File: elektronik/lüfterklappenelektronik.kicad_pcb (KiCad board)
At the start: 2 copper layers, 26 parts, among them P101 CONN_01X04, P103 PressureSensor3, P104 PressureSensor2, P105 PressureSensor1, P106 DamperMotor1, P107 DamperMotor2, P108 DamperMotor3, P109 CONN_01X03, Q101 IRF9540N, Q102 IRF9540N, Q103 IRF9540N, U101 Gabellichtschranke, U102 Gabellichtschranke, U103 Gabellichtschranke, U104 ZG3NC-240B, U105 ATMEGA32U4-A

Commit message: some never to be used routing
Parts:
- P103: footprint Pin_Headers:Pin_Header_Straight_1x04 -> Pin_Headers:Pin_Header_Straight_1x06
- P104: value PressureSensor2 -> PressureSensor1; footprint Pin_Headers:Pin_Header_Straight_1x04 -> Pin_Headers:Pin_Header_Straight_1x06
- P105: value PressureSensor1 -> PressureSensor2; footprint Pin_Headers:Pin_Header_Straight_1x04 -> Pin_Headers:Pin_Header_Straight_1x06
- moved P101 6.25 mm to (127.6, 80.0)
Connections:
- P103 pad 1: /PS3SS -> +5V
- P103 pad 2: Net-(P103-Pad2) -> GND
- P103 pad 3: Net-(P103-Pad3) -> /PS3SS
- P104 pad 1: /PS2SS -> +5V
- P104 pad 2: Net-(P103-Pad2) -> GND
- P104 pad 3: Net-(P103-Pad3) -> /PS1SS
- P105 pad 1: /PS1SS -> +5V
- P105 pad 2: Net-(P103-Pad2) -> GND
- P105 pad 3: Net-(P103-Pad3) -> /PS2SS
- U105 pad 10: Net-(P103-Pad3) -> Net-(P103-Pad5)
- U105 pad 11: Net-(P103-Pad4) -> Net-(P103-Pad6)
- U105 pad 9: Net-(P103-Pad2) -> Net-(P103-Pad4)
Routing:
- net +5V: track 0.00 -> 31.8 mm
- net Net-(P103-Pad6): track 0.00 -> 21.9 mm
- net Net-(P103-Pad5): track 0.00 -> 15.6 mm
- net Net-(P103-Pad2): track 13.8 -> 0.00 mm
- net Net-(P103-Pad3): track 12.7 -> 0.00 mm
- net GND: track 45.7 -> 57.9 mm
- net /PJON: track 0.00 -> 11.3 mm
- net /PS2SS: track 23.2 -> 32.2 mm
- net /PS3SS: track 30.0 -> 32.1 mm
- net /PS1SS: track 27.9 -> 27.2 mm

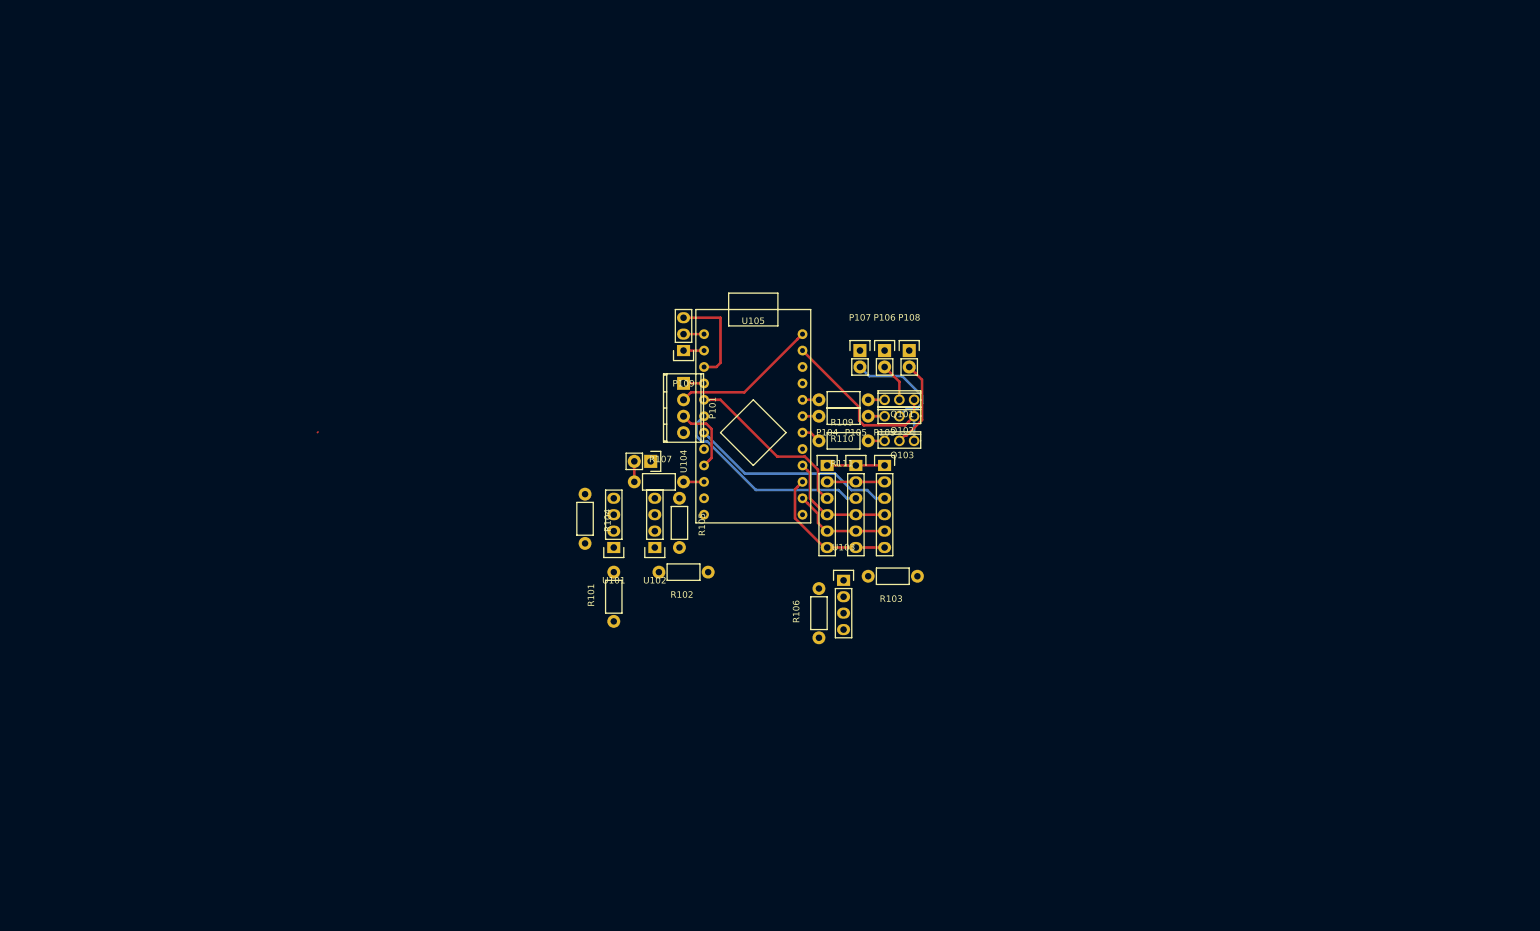
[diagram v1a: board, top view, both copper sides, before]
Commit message: fixed footprints of R and Diode
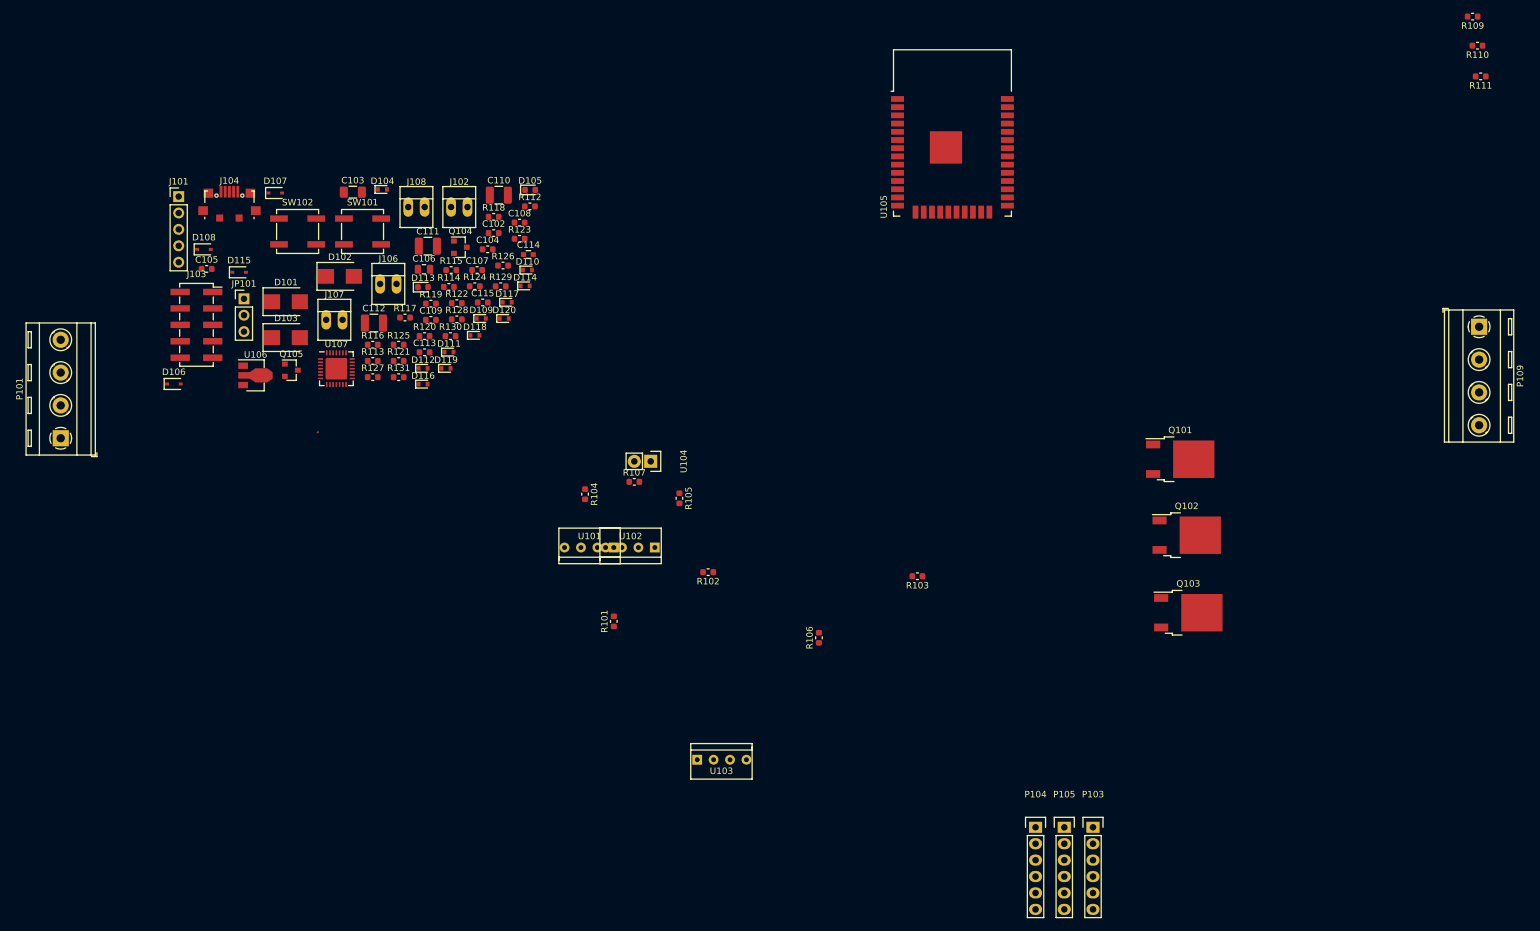
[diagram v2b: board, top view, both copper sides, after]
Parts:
- removed P106: DamperMotor1, Pin_Headers:Pin_Header_Straight_1x02
- removed P107: DamperMotor2, Pin_Headers:Pin_Header_Straight_1x02
- removed P108: DamperMotor3, Pin_Headers:Pin_Header_Straight_1x02
- added C102: 100nF/50V, Capacitor_SMD:C_0603_1608Metric, F.Cu at (98.2, 56.8)
- added C103: 220µF/6.3V(20%), Capacitor_SMD:C_1206_3216Metric, F.Cu at (76.5, 50.4)
- added C104: 100nF/50V, Capacitor_SMD:C_0603_1608Metric, F.Cu at (97.3, 59.3)
- added C105: 1µF/50V, Capacitor_SMD:C_0603_1608Metric, F.Cu at (53.8, 62.3)
- added C106: 10µF/25V, Capacitor_SMD:C_0805_2012Metric, F.Cu at (87.5, 62.4)
- added C107: 100nF/50V, Capacitor_SMD:C_0603_1608Metric, F.Cu at (95.7, 62.5)
- added C108: 100nF/50V, Capacitor_SMD:C_0603_1608Metric, F.Cu at (102.3, 55.1)
- added C109: 100nF/50V, Capacitor_SMD:C_0603_1608Metric, F.Cu at (88.5, 70.2)
- added C110: 22uF/25V(10%), Capacitor_SMD:C_1210_3225Metric, F.Cu at (99.0, 50.9)
- added C111: 22uF/25V(10%), Capacitor_SMD:C_1210_3225Metric, F.Cu at (88.1, 58.8)
- added C112: 22uF/25V(10%), Capacitor_SMD:C_1210_3225Metric, F.Cu at (79.7, 70.7)
- added C113: 100nF/50V, Capacitor_SMD:C_0603_1608Metric, F.Cu at (87.6, 75.2)
- added C114: 4.7µF/6.3V(10%), Capacitors_SMD:C_0603, F.Cu at (103.6, 60.1)
- added C115: 100nF/50V, Capacitor_SMD:C_0603_1608Metric, F.Cu at (96.6, 67.5)
- added D101: D_Schottky, Diode_SMD:D_SMB, F.Cu at (66.1, 67.4)
- added D102: D_Schottky, Diode_SMD:D_SMB, F.Cu at (74.5, 63.5)
- added D103: D_Schottky, Diode_SMD:D_SMB, F.Cu at (66.1, 72.9)
- added D104: LESD5D5.0CT1G, Diode_SMD:D_SOD-523, F.Cu at (81.0, 50.0)
- added D105: GREEN_LED, LED_SMD:LED_0603_1608Metric, F.Cu at (103.9, 50.1)
- added D106: BAT760-7, Diode_SMD:D_SOD-323, F.Cu at (48.8, 80.1)
- added D107: BAT760-7, Diode_SMD:D_SOD-323, F.Cu at (64.5, 50.5)
- added D108: BAT760-7, Diode_SMD:D_SOD-323, F.Cu at (53.4, 59.3)
- added D109: LESD5D5.0CT1G, Diode_SMD:D_SOD-523, F.Cu at (96.3, 70.0)
- added D110: LESD5D5.0CT1G, Diode_SMD:D_SOD-523, F.Cu at (103.5, 62.5)
- added D111: LESD5D5.0CT1G, Diode_SMD:D_SOD-523, F.Cu at (91.3, 75.2)
- added D112: LESD5D5.0CT1G, Diode_SMD:D_SOD-523, F.Cu at (87.3, 77.7)
- added D113: GREEN_LED, LED_SMD:LED_0603_1608Metric, F.Cu at (87.3, 65.1)
- added D114: LESD5D5.0CT1G, Diode_SMD:D_SOD-523, F.Cu at (103.1, 64.9)
- added D115: BAT760-7, Diode_SMD:D_SOD-323, F.Cu at (58.9, 62.8)
- added D116: LESD5D5.0CT1G, Diode_SMD:D_SOD-523, F.Cu at (87.3, 80.1)
- added D117: LESD5D5.0CT1G, Diode_SMD:D_SOD-523, F.Cu at (100.3, 67.5)
- added D118: LESD5D5.0CT1G, Diode_SMD:D_SOD-523, F.Cu at (95.3, 72.6)
- added D119: LESD5D5.0CT1G, Diode_SMD:D_SOD-523, F.Cu at (90.9, 77.7)
- added D120: LESD5D5.0CT1G, Diode_SMD:D_SOD-523, F.Cu at (99.9, 70.0)
- added J101: Conn_01x05_Male, Connector_PinHeader_2.54mm:PinHeader_1x05_P2.54mm_Vertical, F.Cu at (49.5, 51.1)
- added J102: Ckmtw_2510S-2P, Connect:PINHEAD1-2, F.Cu at (91.7, 52.7)
- added J103: Conn_LAN_ENC28J60, Connector_PinSocket_2.54mm:PinSocket_2x05_P2.54mm_Vertical_SMD, F.Cu at (52.3, 71.0)
- added J104: USB_B_Micro, FootprintsTittelbach:USB_Micro-B_C77238, F.Cu at (57.4, 52.0)
- added J106: Ckmtw_2510S-2P, Connect:PINHEAD1-2, F.Cu at (80.7, 64.6)
- added J107: Ckmtw_2510S-2P, Connect:PINHEAD1-2, F.Cu at (72.3, 70.2)
- added J108: Ckmtw_2510S-2P, Connect:PINHEAD1-2, F.Cu at (85.0, 52.7)
- added JP101: Jumper µC Supply, Connector_PinHeader_2.54mm:PinHeader_1x03_P2.54mm_Vertical, F.Cu at (59.6, 66.9)
- added Q104: Q_NPN_Darlington_BEC, Package_TO_SOT_SMD:SOT-23, F.Cu at (93.1, 58.9)
- added Q105: Q_NPN_Darlington_BEC, Package_TO_SOT_SMD:SOT-23, F.Cu at (66.9, 78.0)
- added R112: 110(1%), Resistor_SMD:R_0603_1608Metric, F.Cu at (103.9, 52.6)
- added R113: 0R(5%), Resistor_SMD:R_0603_1608Metric, F.Cu at (79.5, 76.5)
- added R114: 0R(5%), Resistor_SMD:R_0603_1608Metric, F.Cu at (91.3, 65.1)
- added R115: 10K(5%), Resistor_SMD:R_0603_1608Metric, F.Cu at (91.7, 62.5)
- added R116: 10K(5%), Resistor_SMD:R_0603_1608Metric, F.Cu at (79.5, 74.0)
- added R117: 10K(5%), Resistor_SMD:R_0603_1608Metric, F.Cu at (84.5, 69.8)
- added R118: 22(1%), Resistor_SMD:R_0603_1608Metric, F.Cu at (98.2, 54.2)
- added R119: 22(1%), Resistor_SMD:R_0603_1608Metric, F.Cu at (88.5, 67.7)
- added R120: 22(1%), Resistor_SMD:R_0603_1608Metric, F.Cu at (87.6, 72.7)
- added R121: 22(1%), Resistor_SMD:R_0603_1608Metric, F.Cu at (83.5, 76.5)
- added R122: 22(1%), Resistor_SMD:R_0603_1608Metric, F.Cu at (92.5, 67.6)
- added R123: 22(1%), Resistor_SMD:R_0603_1608Metric, F.Cu at (102.3, 57.6)
- added R124: 22(1%), Resistor_SMD:R_0603_1608Metric, F.Cu at (95.3, 65.0)
- added R125: 2K, Resistor_SMD:R_0603_1608Metric, F.Cu at (83.5, 74.0)
- added R126: 22.1K(5%), Resistor_SMD:R_0603_1608Metric, F.Cu at (99.7, 61.8)
- added R127: 47.5K(5%), Resistor_SMD:R_0603_1608Metric, F.Cu at (79.5, 79.0)
- added R128: 2K(5%), Resistor_SMD:R_0603_1608Metric, F.Cu at (92.5, 70.1)
- added R129: 22(1%), Resistor_SMD:R_0603_1608Metric, F.Cu at (99.3, 65.0)
- added R130: 22(1%), Resistor_SMD:R_0603_1608Metric, F.Cu at (91.6, 72.7)
- added R131: 10K(5%), Resistor_SMD:R_0603_1608Metric, F.Cu at (83.5, 79.0)
- added SW101: SW_Push, Button_Switch_SMD:SW_SPST_B3SL-1022P, F.Cu at (78.0, 56.5)
- added SW102: SW_Push, Button_Switch_SMD:SW_SPST_B3SL-1022P, F.Cu at (67.9, 56.5)
- added U106: AMS1117-3.3, Package_TO_SOT_SMD:SOT-89-3, F.Cu at (61.0, 78.8)
- added U107: CP2102N-A01-GQFN28, Package_DFN_QFN:QFN-28-1EP_5x5mm_P0.5mm_EP3.35x3.35mm, F.Cu at (73.9, 77.7)
- P101: value CONN_01X04 -> PWR_BUS_CONN1; footprint Terminal_Blocks:TerminalBlock_Pheonix_MPT-2.54mm_4pol -> TerminalBlock_RND:TerminalBlock_RND_205-00289_1x04_P5.08mm_Horizontal
- P109: value CONN_01X03 -> PWR_BUS_CONN2; footprint Pin_Headers:Pin_Header_Straight_1x03 -> TerminalBlock_RND:TerminalBlock_RND_205-00289_1x04_P5.08mm_Horizontal
- Q101, Q102, Q103: value IRF9540N -> IRLR8743TRPBF; footprint TO_SOT_Packages_THT:TO-251AA -> Package_TO_SOT_SMD:TO-252-2
- R101, R102, R103: value 120 -> 43(1%); footprint Resistors_ThroughHole:Resistor_Horizontal_RM7mm -> Resistor_SMD:R_0603_1608Metric
- R104, R105, R106: footprint Resistors_ThroughHole:Resistor_Horizontal_RM7mm -> Resistor_SMD:R_0603_1608Metric
- R107: value 100 -> 160(1%); footprint Resistors_ThroughHole:Resistor_Horizontal_RM7mm -> Resistor_SMD:R_0603_1608Metric
- R109, R110, R111: value 100 -> 100(1%); footprint Resistors_ThroughHole:Resistor_Horizontal_RM7mm -> Resistor_SMD:R_0603_1608Metric
- U101, U102, U103: footprint Pin_Headers:Pin_Header_Straight_1x04 -> FootprintsTittelbach:Ckmtw_2510S-4P
- U105: value ATMEGA32U4-A -> ESP32-WROOM-32E; footprint ArduinoTeensyFootprints:ArduProMicro -> RF_Module:ESP32-WROOM-32
- moved P109 123.2 mm to (250.8, 71.2), turned to 270 degrees
- moved R109 110.8 mm to (249.8, 23.2)
- moved R110 110.4 mm to (250.5, 27.8)
- moved R111 110.3 mm to (251.0, 32.5)
- moved P101 96.8 mm to (31.2, 88.5), turned to 90 degrees
- moved P103 64.6 mm to (191.0, 148.7)
- moved P104 64.6 mm to (182.1, 148.7)
- moved P105 64.6 mm to (186.6, 148.7)
- moved Q103 54.0 mm to (205.8, 115.5)
- moved Q102 50.2 mm to (205.5, 103.5)
- moved Q101 46.7 mm to (204.5, 91.8)
- moved U105 40.1 mm to (169.2, 44.2)
- moved U103 35.8 mm to (129.8, 138.2)
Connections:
- P101 pad 1: GND -> +12V
- P101 pad 2: +5V -> /PJON
- P101 pad 3: /PJON -> +5V
- P101 pad 4: +12V -> GND
- P103 pad 1: +5V -> +3V3
- P103 pad 3: /PS3SS -> /SCK
- P103 pad 4: Net-(P103-Pad4) -> /MOSI
- P103 pad 5: Net-(P103-Pad5) -> /PS3_CS
- P103 pad 6: Net-(P103-Pad6) -> /MISO
- P104 pad 1: +5V -> +3V3
- P104 pad 3: /PS1SS -> /SCK
- P104 pad 4: Net-(P103-Pad4) -> /MOSI
- P104 pad 5: Net-(P103-Pad5) -> /PS1_CS
- P104 pad 6: Net-(P103-Pad6) -> /MISO
- P105 pad 1: +5V -> +3V3
- P105 pad 3: /PS2SS -> /SCK
- P105 pad 4: Net-(P103-Pad4) -> /MOSI
- P105 pad 5: Net-(P103-Pad5) -> /PS2_CS
- P105 pad 6: Net-(P103-Pad6) -> /MISO
- P109 pad 1: /RX -> GND
- P109 pad 2: /TX -> +5V
- P109 pad 3: GND -> /PJON
- Q101 pad 1: Net-(Q101-Pad1) -> Net-(D101-Pad2)
- Q101 pad 2: Net-(D101-Pad2) -> Net-(Q101-Pad2)
- Q102 pad 1: Net-(Q102-Pad1) -> Net-(D102-Pad2)
- Q102 pad 2: Net-(D102-Pad2) -> Net-(Q102-Pad2)
- Q103 pad 1: Net-(Q103-Pad1) -> Net-(D103-Pad2)
- Q103 pad 2: Net-(D103-Pad2) -> Net-(Q103-Pad2)
- R101 pad 1: +5V -> +3V3
- R102 pad 1: +5V -> +3V3
- R103 pad 1: +5V -> +3V3
- R107 pad 1: Net-(R107-Pad1) -> Net-(D104-Pad1)
- R109 pad 1: Net-(Q101-Pad1) -> Net-(Q101-Pad2)
- R110 pad 1: Net-(Q102-Pad1) -> Net-(Q102-Pad2)
- R111 pad 1: Net-(Q103-Pad1) -> Net-(Q103-Pad2)
- U101 pad 3: /EndstopDamper1 -> Net-(D106-Pad1)
- U102 pad 3: /EndstopDamper2 -> Net-(D107-Pad1)
- U103 pad 3: /EndstopDamper3 -> Net-(D108-Pad1)
- U104 pad 4: Net-(R107-Pad1) -> (no net)
- U105 pad 1: /FAN -> GND
- U105 pad 10: Net-(P103-Pad5) -> /FAN
- U105 pad 11: Net-(P103-Pad6) -> Net-(R121-Pad2)
- U105 pad 13: (no net) -> Net-(R122-Pad2)
- U105 pad 14: +5V -> Net-(R124-Pad2)
- U105 pad 18: /PS2SS -> (no net)
- U105 pad 19: /PS1SS -> (no net)
- U105 pad 20: /RX -> (no net)
- U105 pad 21: /TX -> (no net)
- U105 pad 23: GND -> /LAN_CS
- U105 pad 25: /PS3SS -> /IO0
- U105 pad 27: /PJON -> /LAN_RESET
- U105 pad 29: /EndstopDamper2 -> (no net)
- U105 pad 30: /EndstopDamper3 -> /EndstopDamper2
- U105 pad 31: (no net) -> /EndstopDamper3
- U105 pad 35: GND -> /TXD0
- U105 pad 36: (no net) -> /Damper2
- U105 pad 38: /Damper2 -> GND
- U105 pad 39: /Damper1 -> GND
- U105 pad 7: +5V -> (no net)
- U105 pad 9: Net-(P103-Pad4) -> Net-(R118-Pad1)
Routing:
- net GND: track 57.9 -> 0.00 mm
- net /PS2SS: track 32.2 -> 0.00 mm
- net /PS3SS: track 32.1 -> 0.00 mm
- net +5V: track 31.8 -> 0.00 mm
- net /PS1SS: track 27.2 -> 0.00 mm
- net Net-(P103-Pad6): track 21.9 -> 0.00 mm
- net Net-(P103-Pad4): track 18.2 -> 0.00 mm
- net Net-(D102-Pad2): track 17.0 -> 0.00 mm
- net Net-(P103-Pad5): track 15.6 -> 0.00 mm
- net Net-(D103-Pad2): track 13.9 -> 0.00 mm
- net /PJON: track 11.3 -> 0.00 mm
- net Net-(D101-Pad2): track 6.03 -> 0.00 mm
- net Net-(R107-Pad1): track 3.17 -> 0.00 mm
- net /TX: track 3.17 -> 0.00 mm
- net /RX: track 3.17 -> 0.00 mm
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
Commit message: ready to layout
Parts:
- removed U104: ZG3NC-240B, Pin_Headers:Pin_Header_Straight_1x02
- moved D103 136.7 mm to (190.5, 129.5)
- moved U106 125.0 mm to (137.2, -20.3)
- moved J108 124.4 mm to (189.2, 120.7)
- moved C113 121.5 mm to (172.7, -11.4), turned to 90 degrees
- moved D102 120.0 mm to (185.4, 109.2)
- moved D101 120.0 mm to (185.4, 80.0)
- moved C112 116.6 mm to (161.3, -12.7), turned to 90 degrees
- moved J107 116.2 mm to (184.2, 101.6)
- moved D113 114.2 mm to (149.9, -30.5)
- moved R113 111.8 mm to (185.4, 40.6), turned to 180 degrees
- moved J106 106.6 mm to (184.2, 90.2)
- moved C106 104.5 mm to (94.0, -41.9)
- moved D104 104.2 mm to (158.8, 119.4)
- moved R125 103.3 mm to (128.3, -19.1)
- moved J102 99.2 mm to (165.1, 119.4)
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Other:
- board text added: "12V | 5V"
- board text added: "3V3 GND SCK MOSI CS MISO"
- board text added: "Boot"
- board text added: "Damper1 Motor"
- board text added: "Damper1ES"
- board text added: "Damper2 Motor"
- board text added: "Damper2ES"
- board text added: "Damper3 Motor"
- board text added: "Damper3ES"
- board text added: "EN"
- board text added: "Fan"
- board text added: "GND 5V PJON 12V"
- board text added: "GND Io0 ETx ERx 3V3"
- board text added: "MISO SCK LanReset GND"
- board text added: "MOSI LanCS 3V3"
- board text added: "Pressure1"
- board text added: "Pressure2"
- board text added: "Pressure3"

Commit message: fix LAN port
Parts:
- P101, P109: footprint TerminalBlock_RND:TerminalBlock_RND_205-00289_1x04_P5.08mm_Horizontal -> FootprintsTittelbach:WJ2EDGRC-5.08-4P
- moved J103 229.3 mm to (245.1, 36.8), turned to 270 degrees
- moved D110 130.9 mm to (141.0, 174.0)
- moved D111 124.6 mm to (151.1, 177.8)
- moved D114 124.6 mm to (167.6, 195.6)
- moved R118 124.6 mm to (160.0, 170.2)
- moved R120 124.6 mm to (160.0, 174.0)
- moved R121 124.6 mm to (154.9, 172.7)
- moved R123 124.6 mm to (171.4, 186.7)
- moved D112 124.6 mm to (156.2, 161.3)
- moved D117 124.6 mm to (152.4, 182.9)
- moved R119 124.6 mm to (160.0, 165.1)
- moved R122 124.6 mm to (158.8, 179.1)
- moved D109 124.6 mm to (148.6, 167.6)
- moved R124 124.6 mm to (162.6, 185.4)
- moved U105 52.5 mm to (116.8, 47.0)
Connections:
- J103 pad 10: +3V3 -> GND
- J103 pad 3: /MISO -> (no net)
- J103 pad 4: (no net) -> /MISO
- J103 pad 5: /SCK -> /MOSI
- J103 pad 6: /MOSI -> /SCK
- J103 pad 7: /LAN_RESET -> /LAN_CS
- J103 pad 8: /LAN_CS -> /LAN_RESET
- J103 pad 9: GND -> +3V3

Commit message: place some groups
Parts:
- moved R109 208.0 mm to (12.7, 130.8)
- moved Q101 198.6 mm to (11.4, 138.4), turned to 270 degrees
- moved J102 192.7 mm to (-25.4, 148.6)
- moved D101 186.6 mm to (11.4, 147.3)
- moved J106 185.7 mm to (10.2, 154.9)
- moved R107 181.1 mm to (-20.3, 148.6), turned to 90 degrees
- moved D104 178.9 mm to (-17.8, 148.6), turned to 90 degrees
- moved R110 163.3 mm to (58.4, 141.0), turned to 90 degrees
- moved Q102 158.9 mm to (50.8, 139.7), turned to 180 degrees
- moved J101 153.3 mm to (154.9, 41.9)
- moved J107 148.4 mm to (45.7, 154.9)
- moved D102 144.8 mm to (45.7, 147.3)
- moved R111 136.8 mm to (85.1, 144.8), turned to 270 degrees
- moved Q103 126.6 mm to (81.3, 138.4), turned to 180 degrees
- moved J108 119.3 mm to (74.9, 154.9)
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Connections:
- Q101 pad 1: Net-(D101-Pad2) -> Net-(Q101-Pad1)
- Q101 pad 2: Net-(Q101-Pad2) -> Net-(D101-Pad2)
- Q102 pad 1: Net-(D102-Pad2) -> Net-(Q102-Pad1)
- Q102 pad 2: Net-(Q102-Pad2) -> Net-(D102-Pad2)
- Q103 pad 1: Net-(D103-Pad2) -> Net-(Q103-Pad1)
- Q103 pad 2: Net-(Q103-Pad2) -> Net-(D103-Pad2)
- R109 pad 1: Net-(Q101-Pad2) -> Net-(Q101-Pad1)
- R110 pad 1: Net-(Q102-Pad2) -> Net-(Q102-Pad1)
- R111 pad 1: Net-(Q103-Pad2) -> Net-(Q103-Pad1)
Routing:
- net /UCD-: track 0.00 -> 10.7 mm
- net /UCD+: track 0.00 -> 9.87 mm
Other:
- copper layers 2 -> 4
- board text added: "Damper1 Endstop"
- board text added: "Endstop Damper2"
- board text removed: "Damper1ES"
- board text removed: "Damper2ES"

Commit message: rough placing
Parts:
- J106, J107, J108: value Ckmtw_2510S-2P -> WJ2EDGRC-5.08-2P; footprint Connect:PINHEAD1-2 -> FootprintsTittelbach:WJ2EDGRC-5.08-2P
- moved Q104 168.1 mm to (151.1, -2.54)
- moved Q105 168.1 mm to (151.1, -10.2)
- moved R117 156.8 mm to (146.1, -11.4), turned to 180 degrees
- moved R116 151.6 mm to (146.1, -3.81), turned to 180 degrees
- moved D104 135.2 mm to (104.1, 90.2)
- moved R107 134.0 mm to (100.3, 90.2)
- moved J102 133.7 mm to (97.8, 96.5)
- moved D113 121.1 mm to (100.3, 80.0), turned to 180 degrees
- moved R113 120.2 mm to (130.8, 41.9), turned to 0 degrees
- moved C105 120.0 mm to (94.0, -50.8)
- moved R114 119.4 mm to (130.8, 44.5), turned to 0 degrees
- moved C112 104.1 mm to (109.2, 77.5), turned to 270 degrees
- moved C113 102.9 mm to (113.0, 72.4)
- moved R125 102.8 mm to (96.5, 78.7), turned to 270 degrees
- moved P109 101.7 mm to (149.2, 76.3)
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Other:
- board text added: "BUS"
- board text added: "Damper"
- board text added: "LAN"
- board text added: "USB"
- board text added: "WIFI"
